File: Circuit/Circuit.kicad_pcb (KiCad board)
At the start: 2 copper layers, 28 parts, among them Q2 S8050, Q3 S8050, Q4 S8550, Q5 IRFZ44n, SW1 SW_DPDT_x2, SW2 SW_DPDT_x2, SW3 SW_DPDT_x2, U1 L7805

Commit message: finished PCB
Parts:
- removed D4: SR360, Diode_THT:D_DO-27_P12.70mm_Horizontal
- removed MotorOutput1: TerminalBlock, TerminalBlock:TerminalBlock_bornier-2_P5.08mm
- removed Q2, Q3: S8050, Package_TO_SOT_THT:TO-92_Inline
- removed Q4: S8550, Package_TO_SOT_THT:TO-92_Inline
- removed Q5: IRFZ44n, Package_TO_SOT_THT:TO-220-3_Vertical
- removed R7: 10k, Resistor_THT:R_Axial_DIN0207_L6.3mm_D2.5mm_P7.62mm_Horizontal
- removed R9: 1k, Resistor_THT:R_Axial_DIN0207_L6.3mm_D2.5mm_P7.62mm_Horizontal
- added MotorControl1: JST-2P, Connector_JST:JST_EH_B2B-EH-A_1x02_P2.50mm_Vertical, F.Cu at (178.6, 87.3)
- D1: value LED -> RED
- D2: value LED -> YELLOW
- D3: value LED -> GREEN
- moved SW3 81.7 mm to (183.7, 102.7), turned to 180 degrees
- moved R8 79.5 mm to (183.6, 92.4), turned to 90 degrees
- moved SW1 61.7 mm to (141.3, 104.1), turned to -90 degrees
- moved C1 60.1 mm to (183.1, 71.5), turned to 180 degrees
- moved RV1 55.9 mm to (131.5, 73.9)
- moved SW2 54.8 mm to (141.4, 98.7), turned to -90 degrees
- moved R4 49.6 mm to (152.4, 60.8), turned to -90 degrees
- moved R5 46.7 mm to (133.4, 104.2), turned to 180 degrees
- moved Power24V1 40.2 mm to (178.9, 63.0)
- moved R6 38.6 mm to (133.4, 98.7), turned to 180 degrees
- moved U1 37.8 mm to (178.5, 79.5)
- moved D1 31.4 mm to (130.2, 82.1)
- moved ESP32-CAM1 28.4 mm to (169.6, 102.7), turned to 180 degrees
- moved R1 28.0 mm to (142.2, 82.1)
- moved Debug1 26.2 mm to (176.9, 97.6)
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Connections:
- ESP32-CAM1 pad 1: +5V -> GND
- ESP32-CAM1 pad 2: unconnected-(ESP32-CAM1-Pin_2-Pad2) -> TX
- ESP32-CAM1 pad 3: RED_LED -> RX
- ESP32-CAM1 pad 4: YELLOW_LED -> unconnected-(ESP32-CAM1-Pin_4-Pad4)
- ESP32-CAM1 pad 5: GREEN_LED -> unconnected-(ESP32-CAM1-Pin_5-Pad5)
- ESP32-CAM1 pad 6: SWITCH1 -> BOOT_MODE
- ESP32-CAM1 pad 7: SWITCH2 -> MotorPWM
- ESP32-CAM1 pad 8: POT_ADC -> unconnected-(ESP32-CAM1-Pin_8-Pad8)
- ESP32-CAM2 pad 1: unconnected-(ESP32-CAM2-Pin_1-Pad1) -> SWITCH1
- ESP32-CAM2 pad 2: MotorPWM -> SWITCH2
- ESP32-CAM2 pad 3: BOOT_MODE -> GREEN_LED
- ESP32-CAM2 pad 4: unconnected-(ESP32-CAM2-Pin_4-Pad4) -> RED_LED
- ESP32-CAM2 pad 5: unconnected-(ESP32-CAM2-Pin_5-Pad5) -> YELLOW_LED
- ESP32-CAM2 pad 6: RX -> POT_ADC
- ESP32-CAM2 pad 7: TX -> unconnected-(ESP32-CAM2-Pin_7-Pad7)
- ESP32-CAM2 pad 8: GND -> +5V
- RV1 pad 1: Net-(R4-Pad1) -> GND
- RV1 pad 3: GND -> Net-(R4-Pad1)
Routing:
- net GND: track 0.00 -> 247.0 mm
- net +5V: track 0.00 -> 118.2 mm
- net POT_ADC: track 0.00 -> 39.3 mm
- net Net-(R4-Pad1): track 0.00 -> 22.2 mm
- net BOOT_MODE: track 0.00 -> 20.3 mm
- net +24V: track 0.00 -> 18.5 mm
- net RED_LED: track 0.00 -> 16.2 mm
- net SWITCH2: track 0.00 -> 11.0 mm
- net SWITCH1: track 0.00 -> 9.56 mm
- net MotorPWM: track 0.00 -> 8.99 mm
- net TX: track 0.00 -> 7.35 mm
- net RX: track 0.00 -> 7.35 mm
- net YELLOW_LED: track 0.00 -> 6.39 mm
- net GREEN_LED: track 0.00 -> 6.13 mm
- net Net-(SW3A-C): track 0.00 -> 5.16 mm
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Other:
- board outline added: 64.1 x 49.6 mm
- board text added: "Traffic Controller"

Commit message: fixed PCB, started programming
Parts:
- removed R6: 10K, Resistor_THT:R_Axial_DIN0207_L6.3mm_D2.5mm_P7.62mm_Horizontal
- removed SW2: SW_DPDT_x2, Connector_PinSocket_2.54mm:PinSocket_1x03_P2.54mm_Vertical
- added Proximity1: JST-3p, Connector_JST:JST_EH_B3B-EH-A_1x03_P2.50mm_Vertical, F.Cu at (128.4, 98.3)
- moved R5 0.12 mm to (133.3, 104.0)
- moved SW1 0.12 mm to (141.3, 104.0)
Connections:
- ESP32-CAM2 pad 2: SWITCH2 -> Proximity
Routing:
- net Proximity: track 0.00 -> 14.1 mm
- net GND: track 247.0 -> 233.5 mm
- net SWITCH2: track 11.0 -> 0.00 mm
- net Net-(SW2A-C): track 2.84 -> 0.00 mm
- net +5V: track 118.2 -> 119.6 mm

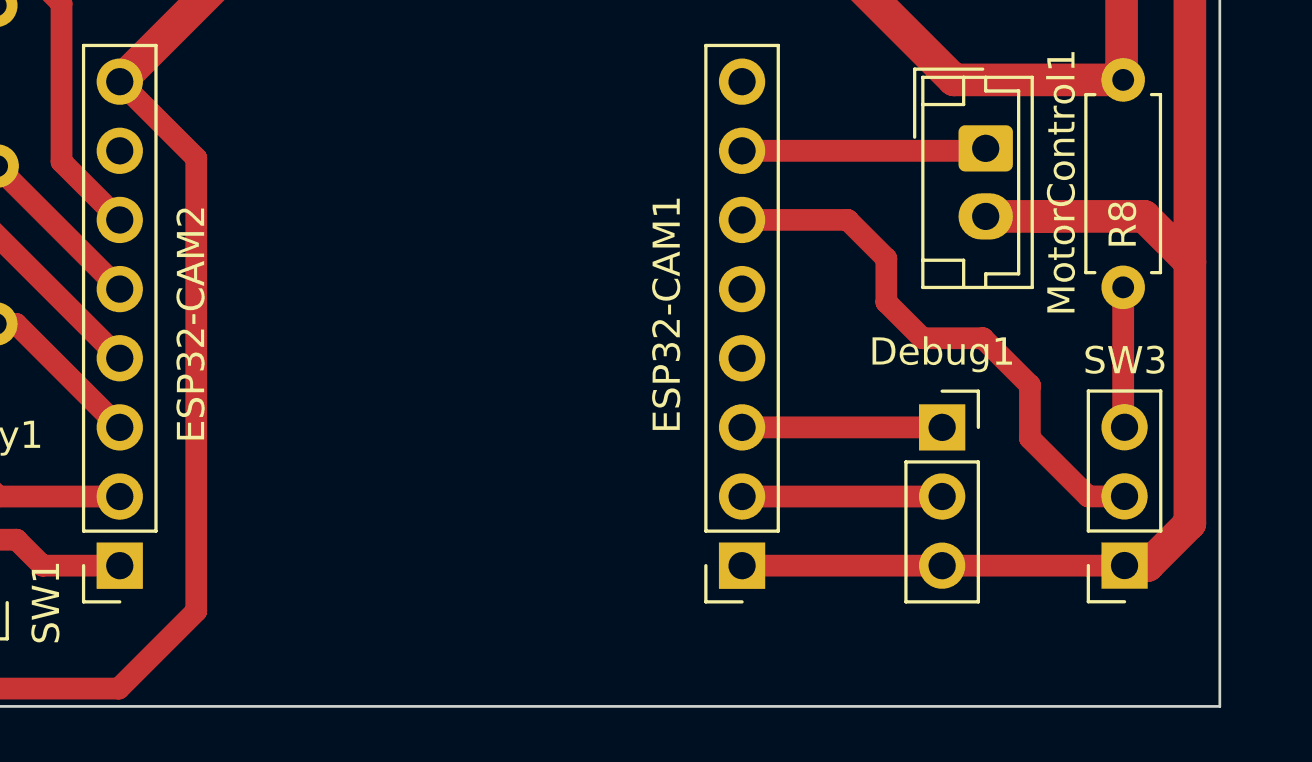
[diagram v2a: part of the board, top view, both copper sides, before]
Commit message: finished Interfacing all sensors and actuators, pending server code
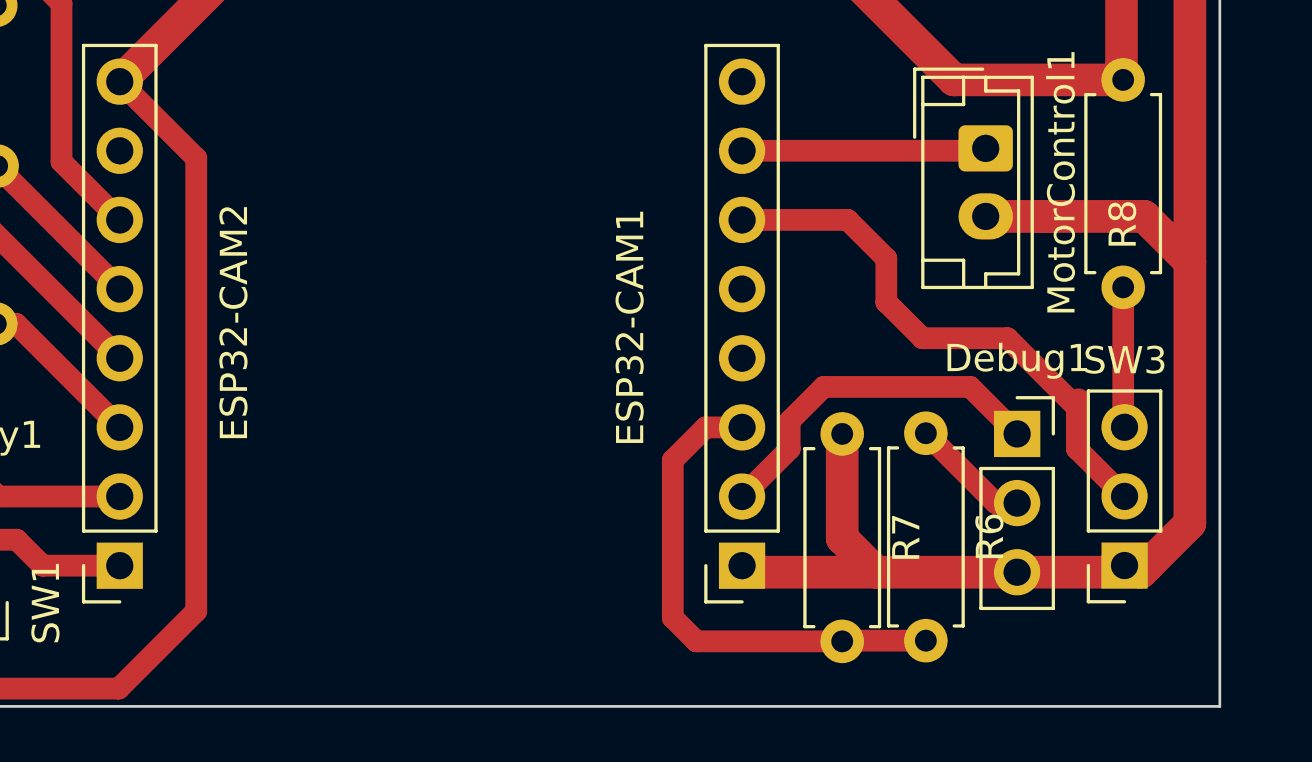
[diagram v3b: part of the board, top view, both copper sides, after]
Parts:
- added R6: 330, Resistor_THT:R_Axial_DIN0207_L6.3mm_D2.5mm_P7.62mm_Horizontal, F.Cu at (176.4, 97.8)
- added R7: 330, Resistor_THT:R_Axial_DIN0207_L6.3mm_D2.5mm_P7.62mm_Horizontal, F.Cu at (173.3, 97.8)
- moved Debug1 2.77 mm to (179.7, 97.8)
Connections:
- Debug1 pad 1: RX -> TX
- Debug1 pad 2: TX -> RX
- ESP32-CAM1 pad 3: RX -> RX_3.3
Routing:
- net RX_3.3: track 0.00 -> 18.5 mm
- net GND: track 233.5 -> 241.3 mm
- net TX: track 7.35 -> 13.4 mm
- net RX: track 7.35 -> 4.42 mm

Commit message: schematic and PCB modification Done
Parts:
- removed MotorControl1: JST-2P, Connector_JST:JST_EH_B2B-EH-A_1x02_P2.50mm_Vertical
- removed RV1: R_Potentiometer, Potentiometer_THT:Potentiometer_Alps_RK163_Single_Horizontal
- removed SW3: SW_DPDT_x2, Connector_PinSocket_2.54mm:PinSocket_1x03_P2.54mm_Vertical
- added Motor1: JST 4P, Connector_JST:JST_EH_B4B-EH-A_1x04_P2.50mm_Vertical, F.Cu at (128.8, 85.1)
- added Q1: S8050, Package_TO_SOT_THT:TO-92_Inline_Wide, F.Cu at (138.2, 96.0)
- added R10: 2k, Resistor_THT:R_Axial_DIN0207_L6.3mm_D2.5mm_P7.62mm_Horizontal, F.Cu at (135.3, 105.6)
- added R9: 1k, Resistor_THT:R_Axial_DIN0207_L6.3mm_D2.5mm_P7.62mm_Horizontal, F.Cu at (141.8, 97.7)
- Proximity1: value JST-3p -> JST 3P
- R4: value ?? -> 1k
- R6: value 330 -> 1k
- R7: value 330 -> 2k
- R8: value 10K -> 2k
- moved R8 50.9 mm to (132.8, 90.1), turned to -90 degrees
- moved R5 50.3 mm to (182.1, 91.6), turned to 90 degrees
- moved R4 42.9 mm to (143.0, 102.6), turned to 180 degrees
- moved SW1 40.0 mm to (176.8, 85.6), turned to 0 degrees
- moved D1 15.7 mm to (130.2, 66.4)
- moved D3 15.7 mm to (130.2, 78.1)
- moved R1 15.7 mm to (142.2, 66.4)
- moved R3 15.7 mm to (142.2, 78.1)
- moved D2 15.7 mm to (130.2, 72.3)
- moved R2 15.7 mm to (142.2, 72.3)
- moved Proximity1 5.95 mm to (126.2, 103.8)
- moved Debug1 2.63 mm to (182.2, 98.7)
- moved R6 1.22 mm to (177.6, 97.7)
- moved R7 1.22 mm to (174.5, 97.7)
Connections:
- ESP32-CAM1 pad 7: MotorPWM -> unconnected-(ESP32-CAM1-Pin_7-Pad7)
- ESP32-CAM2 pad 1: SWITCH1 -> Proximity
- ESP32-CAM2 pad 2: Proximity -> MotorDir1
- ESP32-CAM2 pad 3: GREEN_LED -> MotorPWM
- ESP32-CAM2 pad 6: POT_ADC -> GREEN_LED
- Proximity1 pad 3: Proximity -> Net-(Proximity1-Pin_3)
- R4 pad 1: Net-(R4-Pad1) -> Proximity
- R4 pad 2: +5V -> Net-(Proximity1-Pin_3)
- R8 pad 1: Net-(SW3A-C) -> MotorDir2
- SW1 pad 2: SWITCH1 -> BOOT_MODE
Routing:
- net +5V: track 119.6 -> 168.5 mm
- net POT_ADC: track 39.3 -> 0.00 mm
- net MotorDir1: track 0.00 -> 37.8 mm
- net Net-(R4-Pad1): track 22.2 -> 0.00 mm
- net RED_LED: track 16.2 -> 37.5 mm
- net YELLOW_LED: track 6.39 -> 27.3 mm
- net MotorPWM: track 8.99 -> 28.7 mm
- net GREEN_LED: track 6.13 -> 20.0 mm
- net MotorDir2: track 0.00 -> 13.0 mm
- net BOOT_MODE: track 20.8 -> 7.92 mm
- net SWITCH1: track 9.71 -> 0.00 mm
- net Proximity: track 14.1 -> 6.57 mm
- net TX: track 13.4 -> 18.7 mm
- net Net-(SW3A-C): track 5.16 -> 0.00 mm
- net Net-(Q1-B): track 0.00 -> 5.06 mm
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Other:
- board size 64.1 x 49.6 mm -> 64.5 x 50.3 mm

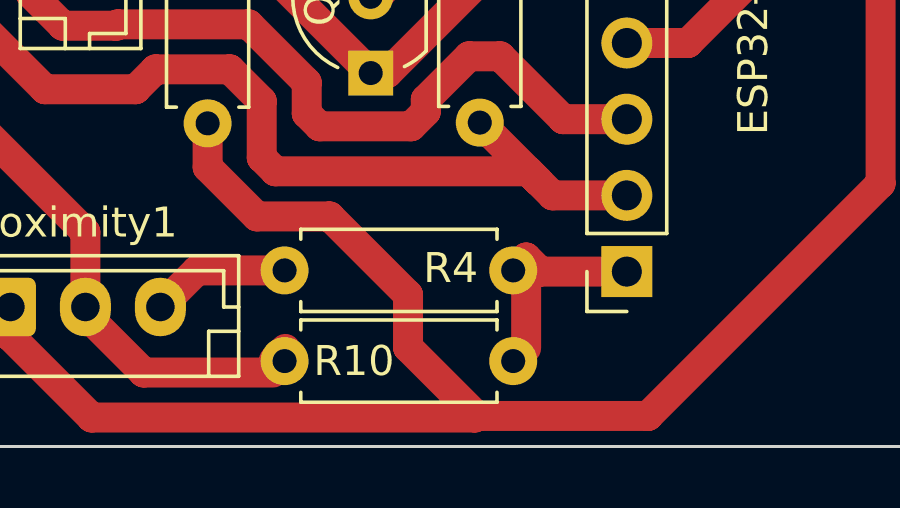
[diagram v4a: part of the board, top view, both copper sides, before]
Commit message: finished and tested Main Routine, pending server socket connection testing
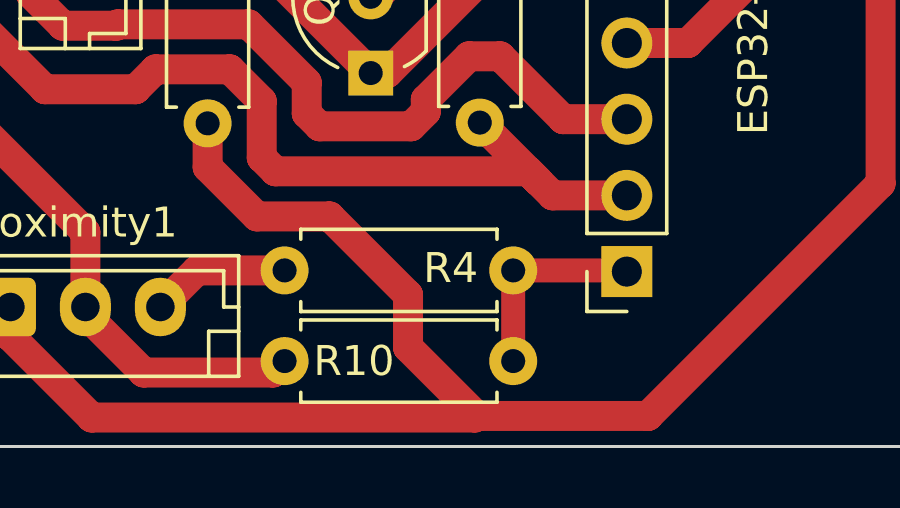
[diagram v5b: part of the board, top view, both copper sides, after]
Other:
- board text added: "the module is upside down ;P"
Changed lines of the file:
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@@
     (effects (font (size 3 3) (thickness 0.5) bold) (justify left bottom))
+  )
+  (gr_text "the module is upside down ;P" (at 160.2994 106.934 90) (layer "F.Fab")
+    (effects (font (size 1 1) (thickness 0.15)) (justify left bottom))
   )
   (dimension (type aligned) (layer "User.3")
@@
   (segment (start 132.7658 97.7138) (end 132.7658 99.17472) (width 1) (layer "F.Cu") (net 1))
   (segment (start 182.0926 84.0232) (end 183.54 82.5758) (width 1) (layer "F.Cu") (net 1))
+  (segment (start 130.634105 106.0196) (end 134.9502 106.0196) (width 1) (layer "F.Cu") (net 2))
   (segment (start 175.7934 100.6602) (end 174.498 99.3648) (width 1) (layer "F.Cu") (net 2))
   (segment (start 127.705 63.9126) (end 127.705 66.4138) (width 1.2) (layer "F.Cu") (net 2))
@@
   (segment (start 144.0942 90.7034) (end 138.7602 96.0374) (width 1) (layer "F.Cu") (net 2))
   (segment (start 179.8066 103.759) (end 179.1208 103.0732) (width 1) (layer "F.Cu") (net 2))
-  (segment (start 134.9756 105.6132) (end 135.3566 105.2322) (width 1) (layer "F.Cu") (net 2))
   (segment (start 183.98 63.05) (end 186.05 65.12) (width 1.2) (layer "F.Cu") (net 2))
   (segment (start 128.7164 103.4288) (end 128.7164 103.670095) (width 1) (layer "F.Cu") (net 2))
@@
   (segment (start 127.705 78.1138) (end 127.705 66.4138) (width 1) (layer "F.Cu") (net 2))
   (segment (start 138.2014 96.0374) (end 134.77364 92.60964) (width 1) (layer "F.Cu") (net 2))
-  (segment (start 130.634105 106.0196) (end 134.9502 106.0196) (width 1) (layer "F.Cu") (net 2))
   (segment (start 181 74.925) (end 181 79.45) (width 1.2) (layer "F.Cu") (net 2))
   (segment (start 144.0942 89.535) (end 144.0942 90.7034) (width 1) (layer "F.Cu") (net 2))
   (segment (start 181.7074 88.7222) (end 186.05 88.7222) (width 1) (layer "F.Cu") (net 2))
+  (segment (start 134.9502 106.0196) (end 135.3312 105.6386) (width 1) (layer "F.Cu") (net 2))
   (segment (start 127.705 79.6482) (end 123.5442 83.809) (width 1) (layer "F.Cu") (net 2))
   (segment (start 131.191 83.1342) (end 137.6934 83.1342) (width 1) (layer "F.Cu") (net 2))
@@
   (segment (start 182.0926 91.6432) (end 177.6984 91.6432) (width 1) (layer "F.Cu") (net 14))
   (segment (start 177.6984 91.6432) (end 176.784 90.7288) (width 1) (layer "F.Cu") (net 14))
-  (segment (start 143.383 102.1842) (end 143.383 105.2068) (width 1) (layer "F.Cu") (net 19))
-  (segment (start 146.74 102.655) (end 143.8538 102.655) (width 1) (layer "F.Cu") (net 19))
-  (segment (start 143.8538 102.655) (end 143.383 102.1842) (width 1) (layer "F.Cu") (net 19))
+  (segment (start 142.9512 102.616) (end 142.9512 105.6386) (width 0.8) (layer "F.Cu") (net 19))
+  (segment (start 146.701 102.616) (end 146.74 102.655) (width 0.8) (layer "F.Cu") (net 19))
+  (segment (start 142.9512 102.616) (end 146.701 102.616) (width 0.8) (layer "F.Cu") (net 19))
   (segment (start 166.7002 105.3338) (end 174.498 105.3338) (width 1) (layer "F.Cu") (net 20))
   (segment (start 167.7026 97.575) (end 165.8874 99.3902) (width 1) (layer "F.Cu") (net 20))
